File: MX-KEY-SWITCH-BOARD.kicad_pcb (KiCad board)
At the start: 2 copper layers, 73 x 54 mm, 36 parts, among them SW1 SW_Push, SW10 SW_Push, SW11 SW_Push, SW12 SW_Push, SW2 SW_Push, SW3 SW_Push, SW4 SW_Push, SW5 SW_Push, SW6 SW_Push, SW7 SW_Push, SW8 SW_Push, SW9 SW_Push

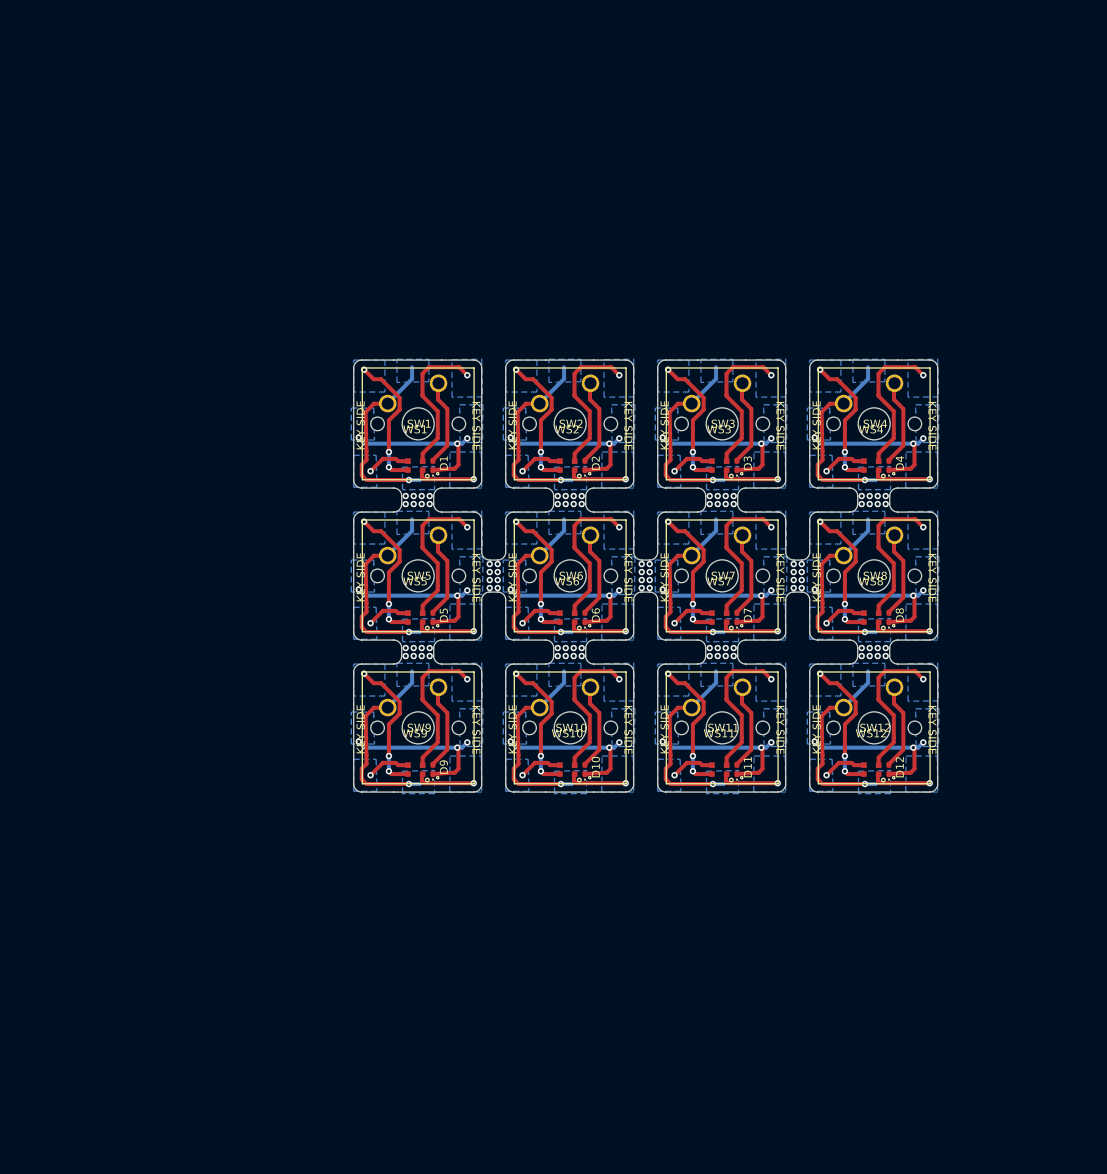
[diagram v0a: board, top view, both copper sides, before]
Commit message: Switching design to add headers to all four sides.
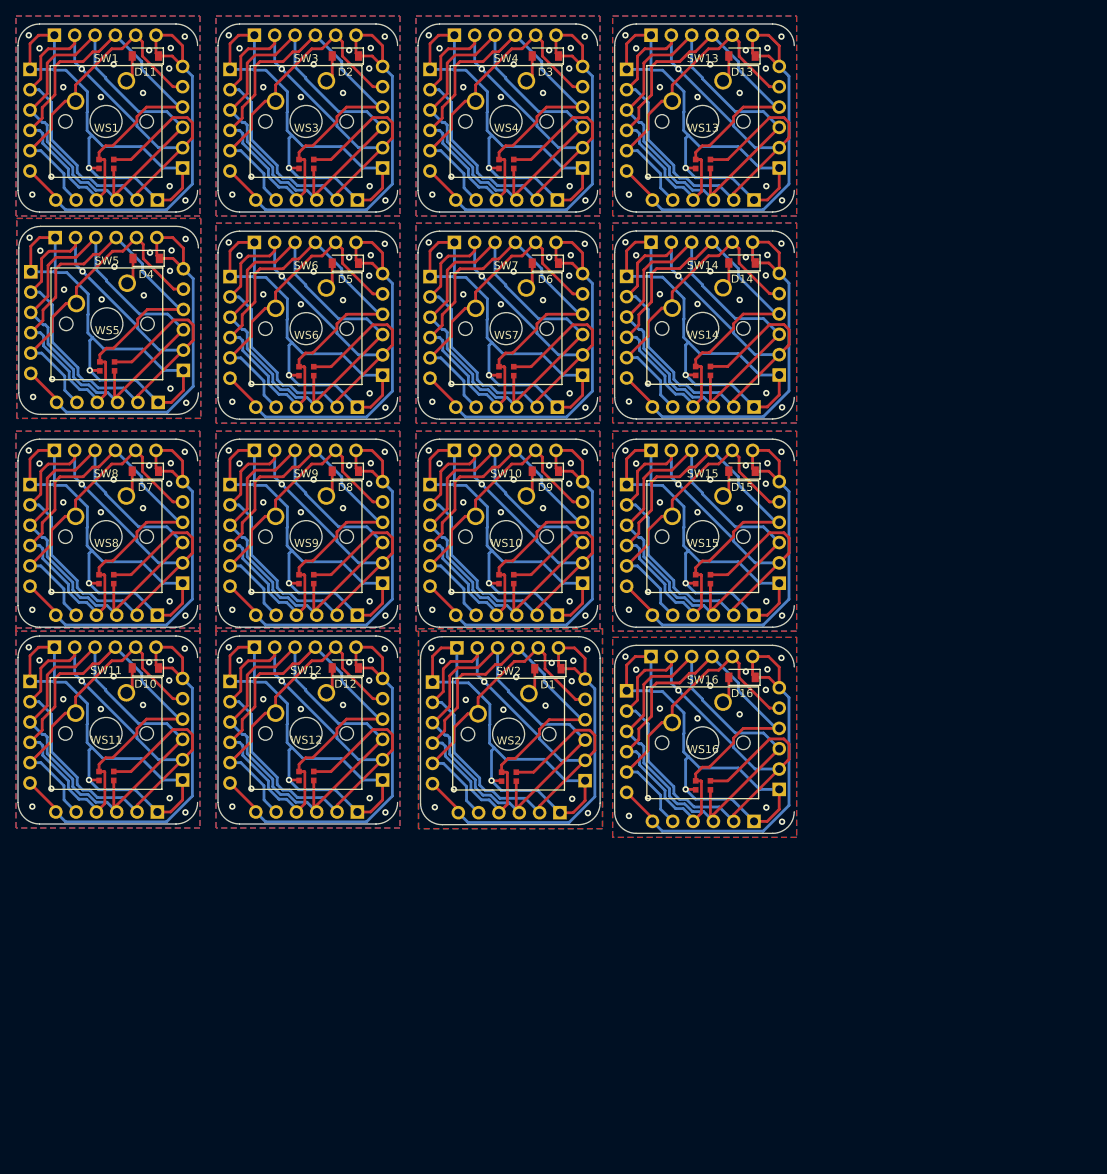
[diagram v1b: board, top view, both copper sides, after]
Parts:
- added D13: 1N4148W, Diode_SMD:D_SOD-123, F.Cu at (40.5, -46.0)
- added D14: 1N4148W, Diode_SMD:D_SOD-123, F.Cu at (40.5, -20.1)
- added D15: 1N4148W, Diode_SMD:D_SOD-123, F.Cu at (40.5, 5.89)
- added D16: 1N4148W, Diode_SMD:D_SOD-123, F.Cu at (40.5, 31.7)
- added J1: Conn_01x06, Connector_PinHeader_2.54mm:PinHeader_1x06_P2.54mm_Vertical, B.Cu at (1.85, 32.3)
- added J10: Conn_01x06, Connector_PinHeader_2.54mm:PinHeader_1x06_P2.54mm_Vertical, B.Cu at (20.6, -32.0)
- added J11: Conn_01x06, Connector_PinHeader_2.54mm:PinHeader_1x06_P2.54mm_Vertical, B.Cu at (4.58, -48.6)
- added J12: Conn_01x06, Connector_PinHeader_2.54mm:PinHeader_1x06_P2.54mm_Vertical, B.Cu at (17.5, -28.0)
- added J13: Conn_01x06, Connector_PinHeader_2.54mm:PinHeader_1x06_P2.54mm_Vertical, B.Cu at (-48.4, -19.0)
- added J14: Conn_01x06, Connector_PinHeader_2.54mm:PinHeader_1x06_P2.54mm_Vertical, B.Cu at (-29.3, -6.71)
- added J15: Conn_01x06, Connector_PinHeader_2.54mm:PinHeader_1x06_P2.54mm_Vertical, B.Cu at (-45.3, -23.3)
- added J16: Conn_01x06, Connector_PinHeader_2.54mm:PinHeader_1x06_P2.54mm_Vertical, B.Cu at (-32.4, -2.71)
- added J17: Conn_01x06, Connector_PinHeader_2.54mm:PinHeader_1x06_P2.54mm_Vertical, B.Cu at (-23.5, -18.4)
- added J18: Conn_01x06, Connector_PinHeader_2.54mm:PinHeader_1x06_P2.54mm_Vertical, B.Cu at (-4.39, -6.11)
- added J19: Conn_01x06, Connector_PinHeader_2.54mm:PinHeader_1x06_P2.54mm_Vertical, B.Cu at (-20.4, -22.7)
- added J2: Conn_01x06, Connector_PinHeader_2.54mm:PinHeader_1x06_P2.54mm_Vertical, B.Cu at (20.9, 44.6)
- added J20: Conn_01x06, Connector_PinHeader_2.54mm:PinHeader_1x06_P2.54mm_Vertical, B.Cu at (-7.54, -2.10)
- added J21: Conn_01x06, Connector_PinHeader_2.54mm:PinHeader_1x06_P2.54mm_Vertical, B.Cu at (1.53, -18.4)
- added J22: Conn_01x06, Connector_PinHeader_2.54mm:PinHeader_1x06_P2.54mm_Vertical, B.Cu at (20.6, -6.11)
- added J23: Conn_01x06, Connector_PinHeader_2.54mm:PinHeader_1x06_P2.54mm_Vertical, B.Cu at (4.58, -22.7)
- added J24: Conn_01x06, Connector_PinHeader_2.54mm:PinHeader_1x06_P2.54mm_Vertical, B.Cu at (17.5, -2.10)
- added J25: Conn_01x06, Connector_PinHeader_2.54mm:PinHeader_1x06_P2.54mm_Vertical, B.Cu at (-48.5, 7.57)
- added J26: Conn_01x06, Connector_PinHeader_2.54mm:PinHeader_1x06_P2.54mm_Vertical, B.Cu at (-29.4, 19.9)
- added J27: Conn_01x06, Connector_PinHeader_2.54mm:PinHeader_1x06_P2.54mm_Vertical, B.Cu at (-45.4, 3.29)
- added J28: Conn_01x06, Connector_PinHeader_2.54mm:PinHeader_1x06_P2.54mm_Vertical, B.Cu at (-32.5, 23.9)
- added J29: Conn_01x06, Connector_PinHeader_2.54mm:PinHeader_1x06_P2.54mm_Vertical, B.Cu at (-23.5, 7.57)
- added J3: Conn_01x06, Connector_PinHeader_2.54mm:PinHeader_1x06_P2.54mm_Vertical, B.Cu at (4.90, 28.0)
- added J30: Conn_01x06, Connector_PinHeader_2.54mm:PinHeader_1x06_P2.54mm_Vertical, B.Cu at (-4.39, 19.9)
- added J31: Conn_01x06, Connector_PinHeader_2.54mm:PinHeader_1x06_P2.54mm_Vertical, B.Cu at (-20.4, 3.29)
- added J32: Conn_01x06, Connector_PinHeader_2.54mm:PinHeader_1x06_P2.54mm_Vertical, B.Cu at (-7.54, 23.9)
- added J33: Conn_01x06, Connector_PinHeader_2.54mm:PinHeader_1x06_P2.54mm_Vertical, B.Cu at (1.53, 7.57)
- added J34: Conn_01x06, Connector_PinHeader_2.54mm:PinHeader_1x06_P2.54mm_Vertical, B.Cu at (20.6, 19.9)
- added J35: Conn_01x06, Connector_PinHeader_2.54mm:PinHeader_1x06_P2.54mm_Vertical, B.Cu at (4.58, 3.29)
- added J36: Conn_01x06, Connector_PinHeader_2.54mm:PinHeader_1x06_P2.54mm_Vertical, B.Cu at (17.5, 23.9)
- added J37: Conn_01x06, Connector_PinHeader_2.54mm:PinHeader_1x06_P2.54mm_Vertical, B.Cu at (-48.5, 32.2)
- added J38: Conn_01x06, Connector_PinHeader_2.54mm:PinHeader_1x06_P2.54mm_Vertical, B.Cu at (-29.4, 44.5)
- added J39: Conn_01x06, Connector_PinHeader_2.54mm:PinHeader_1x06_P2.54mm_Vertical, B.Cu at (-45.4, 27.9)
- added J4: Conn_01x06, Connector_PinHeader_2.54mm:PinHeader_1x06_P2.54mm_Vertical, B.Cu at (17.8, 48.6)
- added J40: Conn_01x06, Connector_PinHeader_2.54mm:PinHeader_1x06_P2.54mm_Vertical, B.Cu at (-32.5, 48.5)
- added J41: Conn_01x06, Connector_PinHeader_2.54mm:PinHeader_1x06_P2.54mm_Vertical, B.Cu at (-48.5, -44.3)
- added J42: Conn_01x06, Connector_PinHeader_2.54mm:PinHeader_1x06_P2.54mm_Vertical, B.Cu at (-29.4, -32.0)
- added J43: Conn_01x06, Connector_PinHeader_2.54mm:PinHeader_1x06_P2.54mm_Vertical, B.Cu at (-45.4, -48.6)
- added J44: Conn_01x06, Connector_PinHeader_2.54mm:PinHeader_1x06_P2.54mm_Vertical, B.Cu at (-32.5, -28.0)
- added J45: Conn_01x06, Connector_PinHeader_2.54mm:PinHeader_1x06_P2.54mm_Vertical, B.Cu at (-23.5, 32.2)
- added J46: Conn_01x06, Connector_PinHeader_2.54mm:PinHeader_1x06_P2.54mm_Vertical, B.Cu at (-4.39, 44.5)
- added J47: Conn_01x06, Connector_PinHeader_2.54mm:PinHeader_1x06_P2.54mm_Vertical, B.Cu at (-20.4, 27.9)
- added J48: Conn_01x06, Connector_PinHeader_2.54mm:PinHeader_1x06_P2.54mm_Vertical, B.Cu at (-7.54, 48.5)
- added J49: Conn_01x06, Connector_PinHeader_2.54mm:PinHeader_1x06_P2.54mm_Vertical, B.Cu at (26.1, -44.3)
- added J5: Conn_01x06, Connector_PinHeader_2.54mm:PinHeader_1x06_P2.54mm_Vertical, B.Cu at (-23.5, -44.3)
- added J50: Conn_01x06, Connector_PinHeader_2.54mm:PinHeader_1x06_P2.54mm_Vertical, B.Cu at (45.2, -32.0)
- added J51: Conn_01x06, Connector_PinHeader_2.54mm:PinHeader_1x06_P2.54mm_Vertical, B.Cu at (29.2, -48.6)
- added J52: Conn_01x06, Connector_PinHeader_2.54mm:PinHeader_1x06_P2.54mm_Vertical, B.Cu at (42.0, -28.0)
- added J53: Conn_01x06, Connector_PinHeader_2.54mm:PinHeader_1x06_P2.54mm_Vertical, B.Cu at (26.1, -18.5)
- added J54: Conn_01x06, Connector_PinHeader_2.54mm:PinHeader_1x06_P2.54mm_Vertical, B.Cu at (45.2, -6.13)
- added J55: Conn_01x06, Connector_PinHeader_2.54mm:PinHeader_1x06_P2.54mm_Vertical, B.Cu at (29.2, -22.7)
- added J56: Conn_01x06, Connector_PinHeader_2.54mm:PinHeader_1x06_P2.54mm_Vertical, B.Cu at (42.0, -2.13)
- added J57: Conn_01x06, Connector_PinHeader_2.54mm:PinHeader_1x06_P2.54mm_Vertical, B.Cu at (26.1, 7.57)
- added J58: Conn_01x06, Connector_PinHeader_2.54mm:PinHeader_1x06_P2.54mm_Vertical, B.Cu at (45.2, 19.9)
- added J59: Conn_01x06, Connector_PinHeader_2.54mm:PinHeader_1x06_P2.54mm_Vertical, B.Cu at (29.2, 3.29)
- added J6: Conn_01x06, Connector_PinHeader_2.54mm:PinHeader_1x06_P2.54mm_Vertical, B.Cu at (-4.39, -32.0)
- added J60: Conn_01x06, Connector_PinHeader_2.54mm:PinHeader_1x06_P2.54mm_Vertical, B.Cu at (42.0, 23.9)
- added J61: Conn_01x06, Connector_PinHeader_2.54mm:PinHeader_1x06_P2.54mm_Vertical, B.Cu at (26.1, 33.3)
- added J62: Conn_01x06, Connector_PinHeader_2.54mm:PinHeader_1x06_P2.54mm_Vertical, B.Cu at (45.2, 45.7)
- added J63: Conn_01x06, Connector_PinHeader_2.54mm:PinHeader_1x06_P2.54mm_Vertical, B.Cu at (29.2, 29.1)
- added J64: Conn_01x06, Connector_PinHeader_2.54mm:PinHeader_1x06_P2.54mm_Vertical, B.Cu at (42.0, 49.7)
- added J7: Conn_01x06, Connector_PinHeader_2.54mm:PinHeader_1x06_P2.54mm_Vertical, B.Cu at (-20.4, -48.6)
- added J8: Conn_01x06, Connector_PinHeader_2.54mm:PinHeader_1x06_P2.54mm_Vertical, B.Cu at (-7.54, -28.0)
- added J9: Conn_01x06, Connector_PinHeader_2.54mm:PinHeader_1x06_P2.54mm_Vertical, B.Cu at (1.53, -44.3)
- added SW13: SW_Push, cherry:SW_Cherry_MX_1.00u_PCB, F.Cu at (38.2, -42.9)
- added SW14: SW_Push, cherry:SW_Cherry_MX_1.00u_PCB, F.Cu at (38.2, -17.0)
- added SW15: SW_Push, cherry:SW_Cherry_MX_1.00u_PCB, F.Cu at (38.2, 8.99)
- added SW16: SW_Push, cherry:SW_Cherry_MX_1.00u_PCB, F.Cu at (38.2, 34.8)
- added WS13: WS2812B-2020-JLCPCB, WingCustomParts:ws2812b-2020-2.0mmx2.0mm, F.Cu at (35.7, -32.5)
- added WS14: WS2812B-2020-JLCPCB, WingCustomParts:ws2812b-2020-2.0mmx2.0mm, F.Cu at (35.7, -6.63)
- added WS15: WS2812B-2020-JLCPCB, WingCustomParts:ws2812b-2020-2.0mmx2.0mm, F.Cu at (35.7, 19.4)
- added WS16: WS2812B-2020-JLCPCB, WingCustomParts:ws2812b-2020-2.0mmx2.0mm, F.Cu at (35.7, 45.2)
- D1, D10, D11, D12, D2, D3, D4, D5, D6, D7, D8, D9: value D -> 1N4148W; footprint Diode_SMD:D_0402_1005Metric_Pad0.77x0.64mm_HandSolder -> Diode_SMD:D_SOD-123
- moved D11 115.8 mm to (-34.0, -46.0), turned to 180 degrees
- moved D4 96.4 mm to (-33.9, -20.7), turned to 180 degrees
- moved SW8 96.1 mm to (-36.4, 8.99)
- moved WS8 95.7 mm to (-38.9, 19.4)
- moved SW11 77.0 mm to (-36.4, 33.6)
- moved WS11 76.6 mm to (-38.9, 44.0)
- moved D7 76.2 mm to (-34.0, 5.89), turned to 180 degrees
- moved SW12 71.0 mm to (-11.4, 33.6)
- moved WS12 70.6 mm to (-13.9, 44.0)
- moved D8 70.4 mm to (-9.04, 5.89), turned to 180 degrees
- moved D12 69.1 mm to (-9.04, 30.5), turned to 180 degrees
- moved SW3 64.3 mm to (-11.4, -42.9)
- moved WS3 63.9 mm to (-13.9, -32.5)
- moved SW4 59.6 mm to (13.6, -42.9)
- moved D2 59.3 mm to (-9.04, -46.0), turned to 180 degrees
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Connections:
- SW1 pad 1: Net-(D1-Pad2) -> Net-(D11-Pad2)
- SW10 pad 1: Net-(D10-Pad2) -> Net-(D9-Pad2)
- SW11 pad 1: Net-(D11-Pad2) -> Net-(D10-Pad2)
- SW2 pad 1: Net-(D2-Pad2) -> Net-(D1-Pad2)
- SW3 pad 1: Net-(D3-Pad2) -> Net-(D2-Pad2)
- SW4 pad 1: Net-(D4-Pad2) -> Net-(D3-Pad2)
- SW5 pad 1: Net-(D5-Pad2) -> Net-(D4-Pad2)
- SW6 pad 1: Net-(D6-Pad2) -> Net-(D5-Pad2)
- SW7 pad 1: Net-(D7-Pad2) -> Net-(D6-Pad2)
- SW8 pad 1: Net-(D8-Pad2) -> Net-(D7-Pad2)
- SW9 pad 1: Net-(D9-Pad2) -> Net-(D8-Pad2)
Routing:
- net GND: track 226.3 -> 1268.1 mm, vias 12 -> 240
- net DI: track 64.1 -> 1036.2 mm, vias 12 -> 0
- net DO: track 89.5 -> 1059.9 mm, vias 12 -> 0
- net VCC: track 214.9 -> 962.4 mm, vias 36 -> 16
- net ROW: track 243.2 -> 828.9 mm, vias 36 -> 0
- net COL: track 295.9 -> 645.4 mm, vias 12 -> 0
- net Net-(D4-Pad2): track 10.9 -> 3.40 mm
- net Net-(D12-Pad2): track 10.9 -> 3.40 mm
- net Net-(D8-Pad2): track 10.9 -> 3.40 mm
- net Net-(D7-Pad2): track 10.9 -> 3.40 mm
- net Net-(D11-Pad2): track 10.9 -> 3.40 mm
- net Net-(D3-Pad2): track 10.9 -> 3.40 mm
- net Net-(D6-Pad2): track 10.9 -> 3.40 mm
- net Net-(D10-Pad2): track 10.9 -> 3.40 mm
- net Net-(D5-Pad2): track 10.9 -> 3.40 mm
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- added copper zone on F.Cu, net GND
- removed copper zone on B.Cu, net COL
- removed copper zone on B.Cu, net DI
- removed copper zone on B.Cu, net DO
- removed copper zone on B.Cu, net ROW
- removed copper zone on B.Cu, net VCC
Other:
- board size 73 x 54 mm -> 97 x 101.2 mm
- board text removed: "COL"
- board text removed: "DI"
- board text removed: "DO"
- board text removed: "GND"
- board text removed: "KEY SIDE"
- board text removed: "ROW"
- board text removed: "VCC"

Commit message: fix
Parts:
- removed J1, J10, J11, J12, J13, J14, J15, J16, J17, J18, J19, J2, J20, J21, J22, J23, J24, J25, J26, J27, J28, J29, J3, J30, J31, J32, J33, J34, J35, J36, J37, J38, J39, J4, J40, J41, J42, J43, J44, J45, J46, J47, J48, J49, J5, J50, J51, J52, J53, J54, J55, J56, J57, J58, J59, J6, J60, J61, J62, J63, J64, J7, J8, J9: Conn_01x06, Connector_PinHeader_2.54mm:PinHeader_1x06_P2.54mm_Vertical
- added BOTTOM1: Conn_01x06, Connector_PinHeader_2.54mm:PinHeader_1x06_P2.54mm_Vertical, F.Cu at (-8.89, 14.7)
- added BOTTOM10: Conn_01x06, Connector_PinHeader_2.54mm:PinHeader_1x06_P2.54mm_Vertical, F.Cu at (16.1, 64.7)
- added BOTTOM11: Conn_01x06, Connector_PinHeader_2.54mm:PinHeader_1x06_P2.54mm_Vertical, F.Cu at (41.1, 64.7)
- added BOTTOM12: Conn_01x06, Connector_PinHeader_2.54mm:PinHeader_1x06_P2.54mm_Vertical, F.Cu at (66.1, 64.7)
- added BOTTOM13: Conn_01x06, Connector_PinHeader_2.54mm:PinHeader_1x06_P2.54mm_Vertical, F.Cu at (-8.89, 89.7)
- added BOTTOM14: Conn_01x06, Connector_PinHeader_2.54mm:PinHeader_1x06_P2.54mm_Vertical, F.Cu at (16.1, 89.7)
- added BOTTOM15: Conn_01x06, Connector_PinHeader_2.54mm:PinHeader_1x06_P2.54mm_Vertical, F.Cu at (41.1, 89.7)
- added BOTTOM16: Conn_01x06, Connector_PinHeader_2.54mm:PinHeader_1x06_P2.54mm_Vertical, F.Cu at (66.1, 89.7)
- added BOTTOM2: Conn_01x06, Connector_PinHeader_2.54mm:PinHeader_1x06_P2.54mm_Vertical, F.Cu at (16.1, 14.7)
- added BOTTOM3: Conn_01x06, Connector_PinHeader_2.54mm:PinHeader_1x06_P2.54mm_Vertical, F.Cu at (41.1, 14.7)
- added BOTTOM4: Conn_01x06, Connector_PinHeader_2.54mm:PinHeader_1x06_P2.54mm_Vertical, F.Cu at (66.1, 14.7)
- added BOTTOM5: Conn_01x06, Connector_PinHeader_2.54mm:PinHeader_1x06_P2.54mm_Vertical, F.Cu at (-8.89, 39.7)
- added BOTTOM6: Conn_01x06, Connector_PinHeader_2.54mm:PinHeader_1x06_P2.54mm_Vertical, F.Cu at (16.1, 39.7)
- added BOTTOM7: Conn_01x06, Connector_PinHeader_2.54mm:PinHeader_1x06_P2.54mm_Vertical, F.Cu at (41.1, 39.7)
- added BOTTOM8: Conn_01x06, Connector_PinHeader_2.54mm:PinHeader_1x06_P2.54mm_Vertical, F.Cu at (66.1, 39.7)
- added BOTTOM9: Conn_01x06, Connector_PinHeader_2.54mm:PinHeader_1x06_P2.54mm_Vertical, F.Cu at (-8.89, 64.7)
- added LEFT1: Conn_01x06, Connector_PinHeader_2.54mm:PinHeader_1x06_P2.54mm_Vertical, F.Cu at (-12.2, -1.27)
- added LEFT10: Conn_01x06, Connector_PinHeader_2.54mm:PinHeader_1x06_P2.54mm_Vertical, F.Cu at (12.8, 48.7)
- added LEFT11: Conn_01x06, Connector_PinHeader_2.54mm:PinHeader_1x06_P2.54mm_Vertical, F.Cu at (37.8, 48.7)
- added LEFT12: Conn_01x06, Connector_PinHeader_2.54mm:PinHeader_1x06_P2.54mm_Vertical, F.Cu at (62.8, 48.7)
- added LEFT13: Conn_01x06, Connector_PinHeader_2.54mm:PinHeader_1x06_P2.54mm_Vertical, F.Cu at (-12.2, 73.7)
- added LEFT14: Conn_01x06, Connector_PinHeader_2.54mm:PinHeader_1x06_P2.54mm_Vertical, F.Cu at (12.8, 73.7)
- added LEFT15: Conn_01x06, Connector_PinHeader_2.54mm:PinHeader_1x06_P2.54mm_Vertical, F.Cu at (37.8, 73.7)
- added LEFT16: Conn_01x06, Connector_PinHeader_2.54mm:PinHeader_1x06_P2.54mm_Vertical, F.Cu at (62.8, 73.7)
- added LEFT2: Conn_01x06, Connector_PinHeader_2.54mm:PinHeader_1x06_P2.54mm_Vertical, F.Cu at (12.8, -1.27)
- added LEFT3: Conn_01x06, Connector_PinHeader_2.54mm:PinHeader_1x06_P2.54mm_Vertical, F.Cu at (37.8, -1.27)
- added LEFT4: Conn_01x06, Connector_PinHeader_2.54mm:PinHeader_1x06_P2.54mm_Vertical, F.Cu at (62.8, -1.27)
- added LEFT5: Conn_01x06, Connector_PinHeader_2.54mm:PinHeader_1x06_P2.54mm_Vertical, F.Cu at (-12.2, 23.7)
- added LEFT6: Conn_01x06, Connector_PinHeader_2.54mm:PinHeader_1x06_P2.54mm_Vertical, F.Cu at (12.8, 23.7)
- added LEFT7: Conn_01x06, Connector_PinHeader_2.54mm:PinHeader_1x06_P2.54mm_Vertical, F.Cu at (37.8, 23.7)
- added LEFT8: Conn_01x06, Connector_PinHeader_2.54mm:PinHeader_1x06_P2.54mm_Vertical, F.Cu at (62.8, 23.7)
- added LEFT9: Conn_01x06, Connector_PinHeader_2.54mm:PinHeader_1x06_P2.54mm_Vertical, F.Cu at (-12.2, 48.7)
- added RIGHT1: Conn_01x06, Connector_PinHeader_2.54mm:PinHeader_1x06_P2.54mm_Vertical, F.Cu at (7.11, 11.4)
- added RIGHT10: Conn_01x06, Connector_PinHeader_2.54mm:PinHeader_1x06_P2.54mm_Vertical, F.Cu at (32.1, 61.4)
- added RIGHT11: Conn_01x06, Connector_PinHeader_2.54mm:PinHeader_1x06_P2.54mm_Vertical, F.Cu at (57.1, 61.4)
- added RIGHT12: Conn_01x06, Connector_PinHeader_2.54mm:PinHeader_1x06_P2.54mm_Vertical, F.Cu at (82.1, 61.4)
- added RIGHT13: Conn_01x06, Connector_PinHeader_2.54mm:PinHeader_1x06_P2.54mm_Vertical, F.Cu at (7.11, 86.4)
- added RIGHT14: Conn_01x06, Connector_PinHeader_2.54mm:PinHeader_1x06_P2.54mm_Vertical, F.Cu at (32.1, 86.4)
- added RIGHT15: Conn_01x06, Connector_PinHeader_2.54mm:PinHeader_1x06_P2.54mm_Vertical, F.Cu at (57.1, 86.4)
- added RIGHT16: Conn_01x06, Connector_PinHeader_2.54mm:PinHeader_1x06_P2.54mm_Vertical, F.Cu at (82.1, 86.4)
- added RIGHT2: Conn_01x06, Connector_PinHeader_2.54mm:PinHeader_1x06_P2.54mm_Vertical, F.Cu at (32.1, 11.4)
- added RIGHT3: Conn_01x06, Connector_PinHeader_2.54mm:PinHeader_1x06_P2.54mm_Vertical, F.Cu at (57.1, 11.4)
- added RIGHT4: Conn_01x06, Connector_PinHeader_2.54mm:PinHeader_1x06_P2.54mm_Vertical, F.Cu at (82.1, 11.4)
- added RIGHT5: Conn_01x06, Connector_PinHeader_2.54mm:PinHeader_1x06_P2.54mm_Vertical, F.Cu at (7.11, 36.4)
- added RIGHT6: Conn_01x06, Connector_PinHeader_2.54mm:PinHeader_1x06_P2.54mm_Vertical, F.Cu at (32.1, 36.4)
- added RIGHT7: Conn_01x06, Connector_PinHeader_2.54mm:PinHeader_1x06_P2.54mm_Vertical, F.Cu at (57.1, 36.4)
- added RIGHT8: Conn_01x06, Connector_PinHeader_2.54mm:PinHeader_1x06_P2.54mm_Vertical, F.Cu at (82.1, 36.4)
- added RIGHT9: Conn_01x06, Connector_PinHeader_2.54mm:PinHeader_1x06_P2.54mm_Vertical, F.Cu at (7.11, 61.4)
- added TOP1: Conn_01x06, Connector_PinHeader_2.54mm:PinHeader_1x06_P2.54mm_Vertical, F.Cu at (3.81, -4.57)
- added TOP10: Conn_01x06, Connector_PinHeader_2.54mm:PinHeader_1x06_P2.54mm_Vertical, F.Cu at (28.8, 45.4)
- added TOP11: Conn_01x06, Connector_PinHeader_2.54mm:PinHeader_1x06_P2.54mm_Vertical, F.Cu at (53.8, 45.4)
- added TOP12: Conn_01x06, Connector_PinHeader_2.54mm:PinHeader_1x06_P2.54mm_Vertical, F.Cu at (78.8, 45.4)
- added TOP13: Conn_01x06, Connector_PinHeader_2.54mm:PinHeader_1x06_P2.54mm_Vertical, F.Cu at (3.81, 70.4)
- added TOP14: Conn_01x06, Connector_PinHeader_2.54mm:PinHeader_1x06_P2.54mm_Vertical, F.Cu at (28.8, 70.4)
- added TOP15: Conn_01x06, Connector_PinHeader_2.54mm:PinHeader_1x06_P2.54mm_Vertical, F.Cu at (53.8, 70.4)
- added TOP16: Conn_01x06, Connector_PinHeader_2.54mm:PinHeader_1x06_P2.54mm_Vertical, F.Cu at (78.8, 70.4)
- added TOP2: Conn_01x06, Connector_PinHeader_2.54mm:PinHeader_1x06_P2.54mm_Vertical, F.Cu at (28.8, -4.57)
- added TOP3: Conn_01x06, Connector_PinHeader_2.54mm:PinHeader_1x06_P2.54mm_Vertical, F.Cu at (53.8, -4.57)
- added TOP4: Conn_01x06, Connector_PinHeader_2.54mm:PinHeader_1x06_P2.54mm_Vertical, F.Cu at (78.8, -4.57)
- added TOP5: Conn_01x06, Connector_PinHeader_2.54mm:PinHeader_1x06_P2.54mm_Vertical, F.Cu at (3.81, 20.4)
- added TOP6: Conn_01x06, Connector_PinHeader_2.54mm:PinHeader_1x06_P2.54mm_Vertical, F.Cu at (28.8, 20.4)
- added TOP7: Conn_01x06, Connector_PinHeader_2.54mm:PinHeader_1x06_P2.54mm_Vertical, F.Cu at (53.8, 20.4)
- added TOP8: Conn_01x06, Connector_PinHeader_2.54mm:PinHeader_1x06_P2.54mm_Vertical, F.Cu at (78.8, 20.4)
- added TOP9: Conn_01x06, Connector_PinHeader_2.54mm:PinHeader_1x06_P2.54mm_Vertical, F.Cu at (3.81, 45.4)
- D1, D10, D11, D12, D13, D14, D15, D16, D2, D3, D4, D5, D6, D7, D8, D9: value 1N4148W -> Diode-SOD323F; footprint Diode_SMD:D_SOD-123 -> Diode_SMD:D_SOD-323F
- moved D13 137.5 mm to (-0.76, 85.2), turned to 90 degrees
- moved D11 134.9 mm to (49.2, 60.2), turned to 90 degrees
- moved WS13 124.1 mm to (-3.30, 85.3)
- moved SW13 123.9 mm to (0.00, 75.0)
- moved SW8 112.6 mm to (75.0, 25.0)
- moved D4 112.5 mm to (74.2, 10.2), turned to 90 degrees
- moved WS8 111.7 mm to (71.7, 35.3)
- moved D14 106.5 mm to (24.2, 85.2), turned to 90 degrees
- moved WS14 93.0 mm to (21.7, 85.3)
- moved SW14 93.0 mm to (25.0, 75.0)
- moved D12 88.4 mm to (74.2, 60.2), turned to 90 degrees
- moved D7 88.3 mm to (49.2, 35.2), turned to 90 degrees
- moved D8 88.3 mm to (74.2, 35.2), turned to 90 degrees
- moved SW11 88.0 mm to (50.0, 50.0)
- moved SW12 88.0 mm to (75.0, 50.0)
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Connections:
- SW1 pad 1: Net-(D11-Pad2) -> Net-(D1-Pad2)
- SW10 pad 1: Net-(D9-Pad2) -> Net-(D10-Pad2)
- SW11 pad 1: Net-(D10-Pad2) -> Net-(D11-Pad2)
- SW2 pad 1: Net-(D1-Pad2) -> Net-(D2-Pad2)
- SW3 pad 1: Net-(D2-Pad2) -> Net-(D3-Pad2)
- SW4 pad 1: Net-(D3-Pad2) -> Net-(D4-Pad2)
- SW5 pad 1: Net-(D4-Pad2) -> Net-(D5-Pad2)
- SW6 pad 1: Net-(D5-Pad2) -> Net-(D6-Pad2)
- SW7 pad 1: Net-(D6-Pad2) -> Net-(D7-Pad2)
- SW8 pad 1: Net-(D7-Pad2) -> Net-(D8-Pad2)
- SW9 pad 1: Net-(D8-Pad2) -> Net-(D9-Pad2)
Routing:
- net GND: track 1268.1 -> 803.5 mm, vias 240 -> 64
- net DO: track 1059.9 -> 698.5 mm, vias 0 -> 16
- net DI: track 1036.2 -> 730.7 mm, vias 0 -> 64
- net VCC: track 962.4 -> 795.2 mm, vias 16 -> 32
- net ROW: track 828.9 -> 672.8 mm, vias 0 -> 32
- net COL: track 645.4 -> 664.1 mm, vias 0 -> 16
- net Net-(D4-Pad2): track 3.40 -> 9.57 mm
- net Net-(D12-Pad2): track 3.40 -> 9.57 mm
- net Net-(D10-Pad2): track 3.40 -> 9.57 mm
- net Net-(D8-Pad2): track 3.40 -> 9.57 mm
- net Net-(D7-Pad2): track 3.40 -> 9.57 mm
- net Net-(D6-Pad2): track 3.40 -> 9.57 mm
- net Net-(D15-Pad2): track 3.40 -> 9.57 mm
- net Net-(D9-Pad2): track 3.40 -> 9.57 mm
- net Net-(D16-Pad2): track 3.40 -> 9.57 mm
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- added copper zone on F.Cu, net VCC
- removed copper zone on F.Cu, net GND
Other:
- board size 97 x 101.2 mm -> 97.9 x 97.9 mm
- board text added: "(C)WINGTECHCORNER.COM"
- board text added: "KEY-SIDE"
- board text added: "MX-COL2ROW WS2812"
